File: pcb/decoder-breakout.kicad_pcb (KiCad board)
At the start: 2 copper layers, 1 part, among them U1 LS7866-S

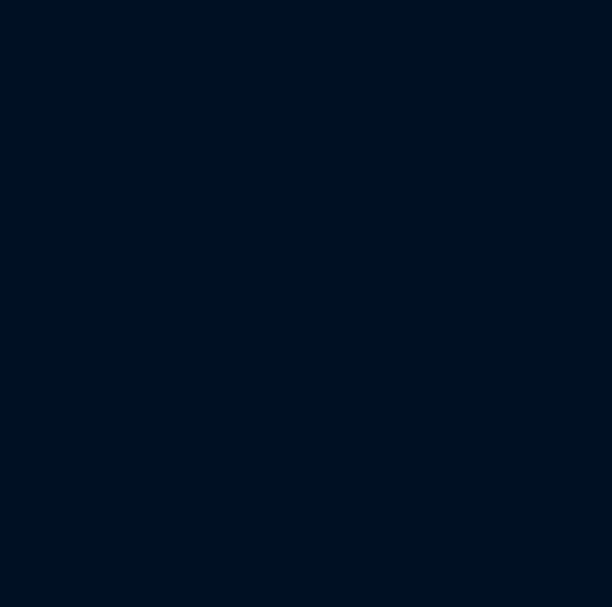
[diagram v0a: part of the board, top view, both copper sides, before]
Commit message: add resistors and jumpers
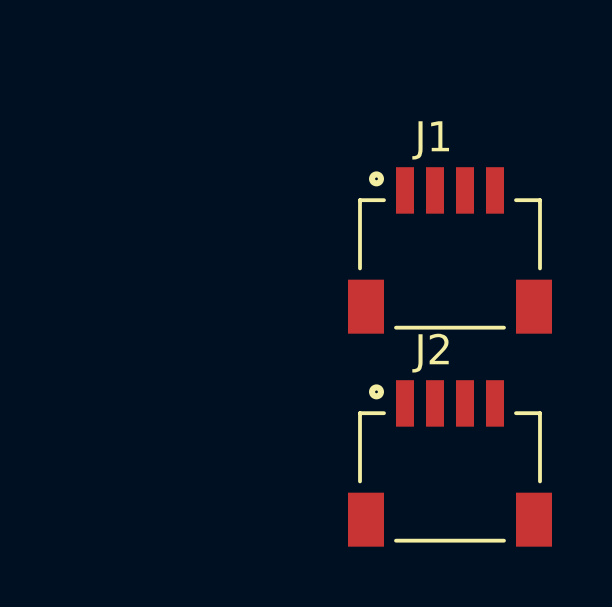
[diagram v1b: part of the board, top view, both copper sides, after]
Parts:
- added J1: SM04B-SRSS-TB_LF__SN_, SM04B-SRSS-TB(LF)(SN):JST_SM04B-SRSS-TB_LF__SN_, F.Cu at (169.9, 83.0)
- added J2: SM04B-SRSS-TB_LF__SN_, SM04B-SRSS-TB(LF)(SN):JST_SM04B-SRSS-TB_LF__SN_, F.Cu at (169.9, 90.1)
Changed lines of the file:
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@@
   (net 13 "unconnected-(U1-~{DFLAG}-Pad13)")
   (net 14 "unconnected-(U1-VDD-Pad14)")
+  (net 15 "unconnected-(J1-Pad1)")
+  (net 16 "unconnected-(J1-Pad2)")
+  (net 17 "unconnected-(J1-Pad3)")
+  (net 18 "unconnected-(J1-Pad4)")
+  (net 19 "Net-(J1-SHIELD-PadS1)")
+  (net 20 "unconnected-(J2-Pad1)")
+  (net 21 "unconnected-(J2-Pad2)")
+  (net 22 "unconnected-(J2-Pad3)")
+  (net 23 "unconnected-(J2-Pad4)")
+  (net 24 "Net-(J2-SHIELD-PadS1)")
   (footprint "LS7866-S:SOIC127P600X175-14N" (layer "F.Cu")
     (at 139.785 85.09)
@@
     (pad "14" smd roundrect (at 2.455 -3.81) (size 1.9 0.6) (layers "F.Cu" "F.Paste" "F.Mask") (roundrect_rratio 0.07)
       (net 14 "unconnected-(U1-VDD-Pad14)") (pinfunction "VDD") (pintype "power_in") (solder_mask_margin 0.102))
+    (model "${KIPRJMOD}/LS7866-S/LS7866-S--3DModel-STEP-56544.STEP"
+      (offset (xyz 0 0 0))
+      (scale (xyz 1 1 1))
+      (rotate (xyz -90 0 0))
+    )
+  )
+  (footprint "SM04B-SRSS-TB(LF)(SN):JST_SM04B-SRSS-TB_LF__SN_" (layer "F.Cu")
+    (at 169.92 90.105)
+    (property "Availability" "In Stock")
+    (property "Check_prices" "https://www.snapeda.com/parts/SM04B-SRSS-TB(LF)(SN)/JST+Sales+America+Inc./view-part/?ref=eda")
+    (property "Description" "\nConnector Header Surface Mount, Right Angle 4 position 0.039 (1.00mm)\n")
+    (property "MANUFACTURER" "JST")
+    (property "MF" "JST Sales")
+    (property "MP" "SM04B-SRSS-TB(LF)(SN)")
+    (property "Package" "None")
+    (property "Price" "None")
+    (property "STANDARD" "Manufacturer recommendations")
+    (property "Sheetfile" "decoder-breakout.kicad_sch")
+    (property "Sheetname" "")
+    (property "SnapEDA_Link" "https://www.snapeda.com/parts/SM04B-SRSS-TB(LF)(SN)/JST+Sales+America+Inc./view-part/?ref=snap")
+    (attr smd)
+    (fp_text reference "J2" (at -0.545095 -1.767685) (layer "F.SilkS")
+        (effects (font (size 1.001173 1.001173) (thickness 0.15)))
+    )
+    (fp_text value "SM04B-SRSS-TB_LF__SN_" (at 12.17039 5.74055) (layer "F.Fab")
+        (effects (font (size 1.000567 1.000567) (thickness 0.15)))
+    )
+    (fp_line (start -3 0.325) (end -3 2.6)
+      (stroke (width 0.127) (type solid)) (layer "F.SilkS"))
+    (fp_line (start -2.2 0.325) (end -3 0.325)
+      (stroke (width 0.127) (type solid)) (layer "F.SilkS"))
+    (fp_line (start -1.8 4.575) (end 1.8 4.575)
+      (stroke (width 0.127) (type solid)) (layer "F.SilkS"))
+    (fp_line (start 2.2 0.325) (end 3 0.325)
+      (stroke (width 0.127) (type solid)) (layer "F.SilkS"))
+    (fp_line (start 3 0.325) (end 3 2.6)
+      (stroke (width 0.127) (type solid)) (layer "F.SilkS"))
+    (fp_circle (center -2.45 -0.385) (end -2.35 -0.385)
+      (stroke (width 0.3) (type solid)) (fill none) (layer "F.SilkS"))
+    (fp_line (start -3.65 -1.025) (end 3.65 -1.025)
+      (stroke (width 0.05) (type solid)) (layer "F.CrtYd"))
+    (fp_line (start -3.65 5.025) (end -3.65 -1.025)
+      (stroke (width 0.05) (type solid)) (layer "F.CrtYd"))
+    (fp_line (start 3.65 -1.025) (end 3.65 5.025)
+      (stroke (width 0.05) (type solid)) (layer "F.CrtYd"))
+    (fp_line (start 3.65 5.025) (end -3.65 5.025)
+      (stroke (width 0.05) (type solid)) (layer "F.CrtYd"))
+    (fp_line (start -3 0.325) (end 3 0.325)
+      (stroke (width 0.127) (type solid)) (layer "F.Fab"))
+    (fp_line (start -3 4.575) (end -3 0.325)
+      (stroke (width 0.127) (type solid)) (layer "F.Fab"))
+    (fp_line (start 3 0.325) (end 3 4.575)
+      (stroke (width 0.127) (type solid)) (layer "F.Fab"))
+    (fp_line (start 3 4.575) (end -3 4.575)
+      (stroke (width 0.127) (type solid)) (layer "F.Fab"))
+    (fp_circle (center -2.45 -0.385) (end -2.35 -0.385)
+      (stroke (width 0.3) (type solid)) (fill none) (layer "F.Fab"))
+    (pad "1" smd rect (at -1.5 0) (size 0.6 1.55) (layers "F.Cu" "F.Paste" "F.Mask")
+      (net 20 "unconnected-(J2-Pad1)") (pinfunction "1") (pintype "passive") (solder_mask_margin 0.102))
+    (pad "2" smd rect (at -0.5 0) (size 0.6 1.55) (layers "F.Cu" "F.Paste" "F.Mask")
+      (net 21 "unconnected-(J2-Pad2)") (pinfunction "2") (pintype "passive") (solder_mask_margin 0.102))
+    (pad "3" smd rect (at 0.5 0) (size 0.6 1.55) (layers "F.Cu" "F.Paste" "F.Mask")
+      (net 22 "unconnected-(J2-Pad3)") (pinfunction "3") (pintype "passive") (solder_mask_margin 0.102))
+    (pad "4" smd rect (at 1.5 0) (size 0.6 1.55) (layers "F.Cu" "F.Paste" "F.Mask")
+      (net 23 "unconnected-(J2-Pad4)") (pinfunction "4") (pintype "passive") (solder_mask_margin 0.102))
+    (pad "S1" smd rect (at -2.8 3.875 180) (size 1.2 1.8) (layers "F.Cu" "F.Paste" "F.Mask")
+      (net 24 "Net-(J2-SHIELD-PadS1)") (pinfunction "SHIELD") (pintype "passive") (solder_mask_margin 0.102))
+    (pad "S2" smd rect (at 2.8 3.875 180) (size 1.2 1.8) (layers "F.Cu" "F.Paste" "F.Mask")
+      (net 24 "Net-(J2-SHIELD-PadS1)") (pinfunction "SHIELD") (pintype "passive") (solder_mask_margin 0.102))
+    (model "${KIPRJMOD}/SM04B-SRSS-TB(LF)(SN)/SM04B-SRSS-TB_LF__SN_.step"
+      (offset (xyz 0 0 -0.3))
+      (scale (xyz 1 1 1))
+      (rotate (xyz -90 0 0))
+    )
+  )
+  (footprint "SM04B-SRSS-TB(LF)(SN):JST_SM04B-SRSS-TB_LF__SN_" (layer "F.Cu")
+    (at 169.92 83.005)
+    (property "Availability" "In Stock")
+    (property "Check_prices" "https://www.snapeda.com/parts/SM04B-SRSS-TB(LF)(SN)/JST+Sales+America+Inc./view-part/?ref=eda")
+    (property "Description" "\nConnector Header Surface Mount, Right Angle 4 position 0.039 (1.00mm)\n")
+    (property "MANUFACTURER" "JST")
+    (property "MF" "JST Sales")
+    (property "MP" "SM04B-SRSS-TB(LF)(SN)")
+    (property "Package" "None")
+    (property "Price" "None")
+    (property "STANDARD" "Manufacturer recommendations")
+    (property "Sheetfile" "decoder-breakout.kicad_sch")
+    (property "Sheetname" "")
+    (property "SnapEDA_Link" "https://www.snapeda.com/parts/SM04B-SRSS-TB(LF)(SN)/JST+Sales+America+Inc./view-part/?ref=snap")
+    (attr smd)
+    (fp_text reference "J1" (at -0.545095 -1.767685) (layer "F.SilkS")
+        (effects (font (size 1.001173 1.001173) (thickness 0.15)))
+    )
+    (fp_text value "SM04B-SRSS-TB_LF__SN_" (at 12.17039 5.74055) (layer "F.Fab")
+        (effects (font (size 1.000567 1.000567) (thickness 0.15)))
+    )
+    (fp_line (start -3 0.325) (end -3 2.6)
+      (stroke (width 0.127) (type solid)) (layer "F.SilkS"))
+    (fp_line (start -2.2 0.325) (end -3 0.325)
+      (stroke (width 0.127) (type solid)) (layer "F.SilkS"))
+    (fp_line (start -1.8 4.575) (end 1.8 4.575)
+      (stroke (width 0.127) (type solid)) (layer "F.SilkS"))
+    (fp_line (start 2.2 0.325) (end 3 0.325)
+      (stroke (width 0.127) (type solid)) (layer "F.SilkS"))
+    (fp_line (start 3 0.325) (end 3 2.6)
+      (stroke (width 0.127) (type solid)) (layer "F.SilkS"))
+    (fp_circle (center -2.45 -0.385) (end -2.35 -0.385)
+      (stroke (width 0.3) (type solid)) (fill none) (layer "F.SilkS"))
+    (fp_line (start -3.65 -1.025) (end 3.65 -1.025)
+      (stroke (width 0.05) (type solid)) (layer "F.CrtYd"))
+    (fp_line (start -3.65 5.025) (end -3.65 -1.025)
+      (stroke (width 0.05) (type solid)) (layer "F.CrtYd"))
+    (fp_line (start 3.65 -1.025) (end 3.65 5.025)
+      (stroke (width 0.05) (type solid)) (layer "F.CrtYd"))
+    (fp_line (start 3.65 5.025) (end -3.65 5.025)
+      (stroke (width 0.05) (type solid)) (layer "F.CrtYd"))
+    (fp_line (start -3 0.325) (end 3 0.325)
+      (stroke (width 0.127) (type solid)) (layer "F.Fab"))
+    (fp_line (start -3 4.575) (end -3 0.325)
+      (stroke (width 0.127) (type solid)) (layer "F.Fab"))
+    (fp_line (start 3 0.325) (end 3 4.575)
+      (stroke (width 0.127) (type solid)) (layer "F.Fab"))
+    (fp_line (start 3 4.575) (end -3 4.575)
+      (stroke (width 0.127) (type solid)) (layer "F.Fab"))
+    (fp_circle (center -2.45 -0.385) (end -2.35 -0.385)
+      (stroke (width 0.3) (type solid)) (fill none) (layer "F.Fab"))
+    (pad "1" smd rect (at -1.5 0) (size 0.6 1.55) (layers "F.Cu" "F.Paste" "F.Mask")
+      (net 15 "unconnected-(J1-Pad1)") (pinfunction "1") (pintype "passive") (solder_mask_margin 0.102))
+    (pad "2" smd rect (at -0.5 0) (size 0.6 1.55) (layers "F.Cu" "F.Paste" "F.Mask")
+      (net 16 "unconnected-(J1-Pad2)") (pinfunction "2") (pintype "passive") (solder_mask_margin 0.102))
+    (pad "3" smd rect (at 0.5 0) (size 0.6 1.55) (layers "F.Cu" "F.Paste" "F.Mask")
+      (net 17 "unconnected-(J1-Pad3)") (pinfunction "3") (pintype "passive") (solder_mask_margin 0.102))
+    (pad "4" smd rect (at 1.5 0) (size 0.6 1.55) (layers "F.Cu" "F.Paste" "F.Mask")
+      (net 18 "unconnected-(J1-Pad4)") (pinfunction "4") (pintype "passive") (solder_mask_margin 0.102))
+    (pad "S1" smd rect (at -2.8 3.875 180) (size 1.2 1.8) (layers "F.Cu" "F.Paste" "F.Mask")
+      (net 19 "Net-(J1-SHIELD-PadS1)") (pinfunction "SHIELD") (pintype "passive") (solder_mask_margin 0.102))
+    (pad "S2" smd rect (at 2.8 3.875 180) (size 1.2 1.8) (layers "F.Cu" "F.Paste" "F.Mask")
+      (net 19 "Net-(J1-SHIELD-PadS1)") (pinfunction "SHIELD") (pintype "passive") (solder_mask_margin 0.102))
+    (model "${KIPRJMOD}/SM04B-SRSS-TB(LF)(SN)/SM04B-SRSS-TB_LF__SN_.step"
+      (offset (xyz 0 0 -0.3))
+      (scale (xyz 1 1 1))
+      (rotate (xyz -90 0 0))
+    )
   )
 )

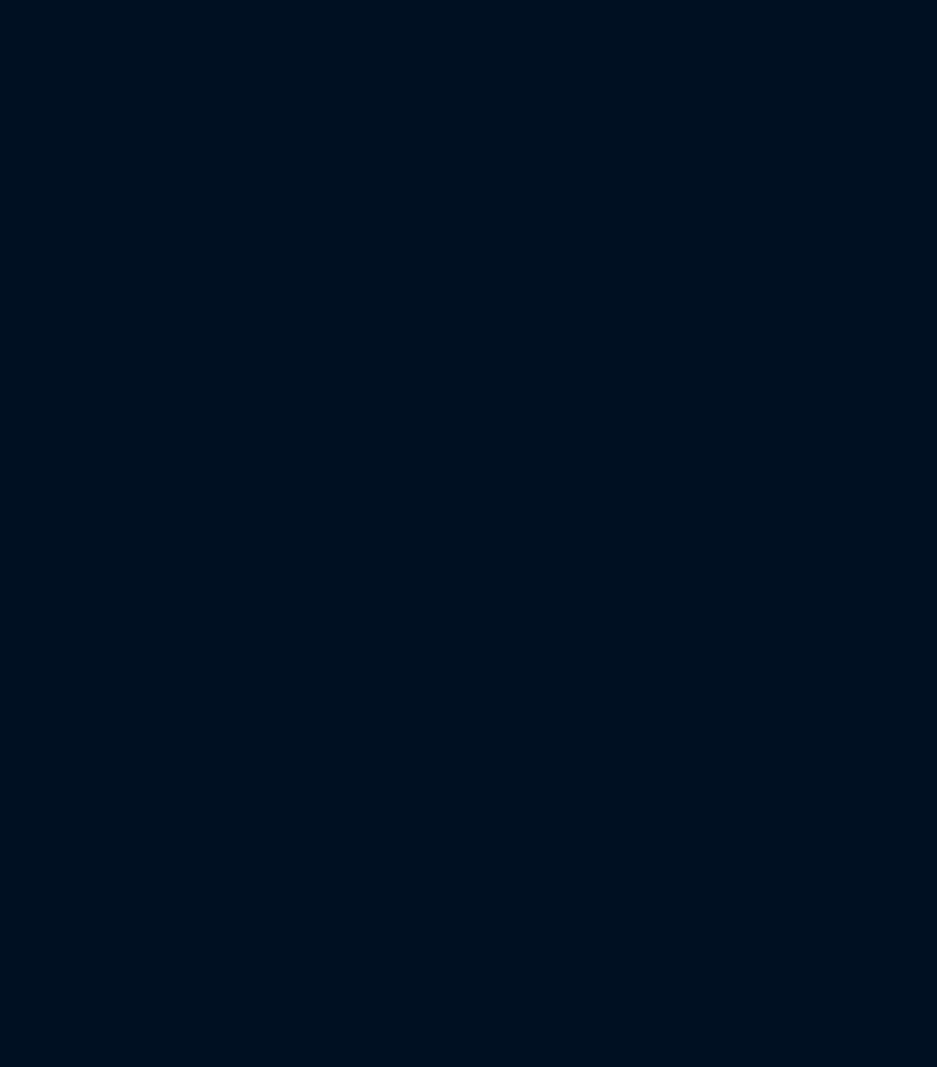
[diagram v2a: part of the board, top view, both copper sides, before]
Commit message: added terminal block, started on PCB
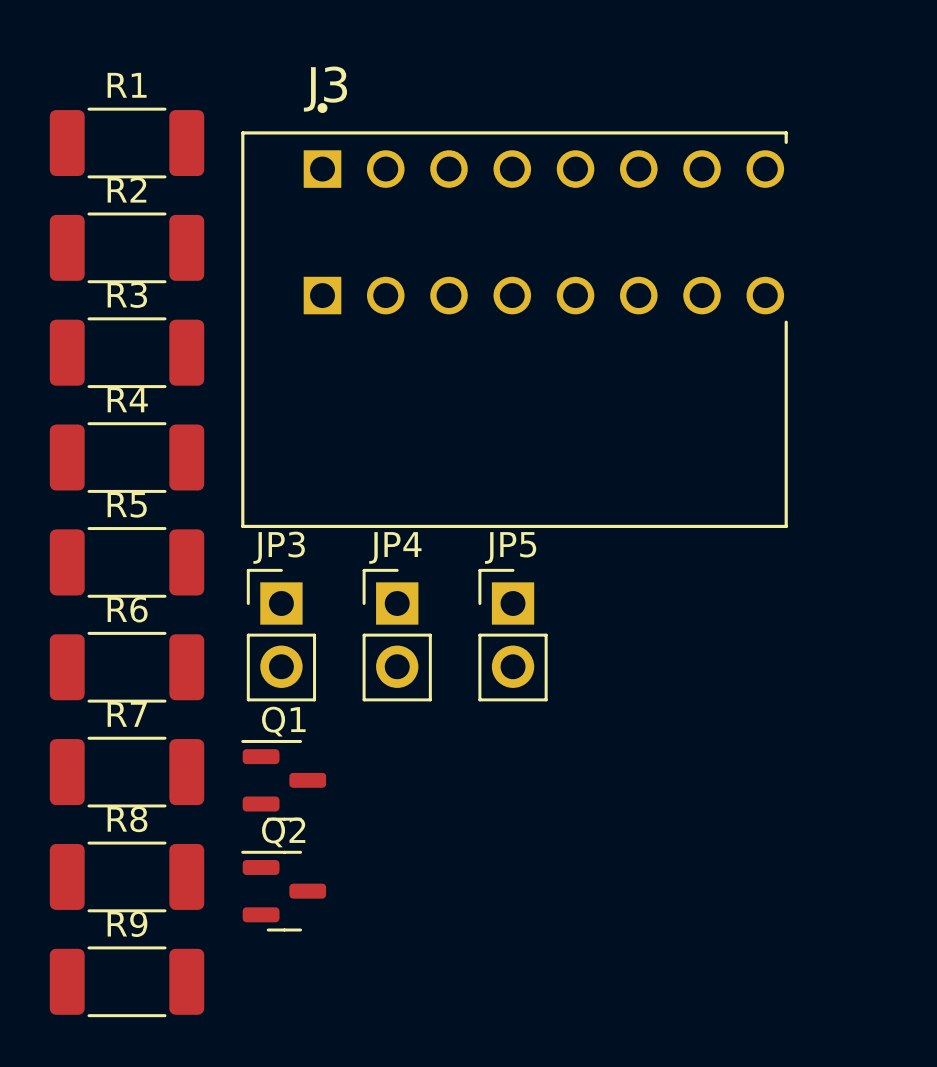
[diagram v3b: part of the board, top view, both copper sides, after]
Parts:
- added J3: TBL009-254-08GY-2GY, TBL009-254-08GY-2GY:CUI_TBL009-254-08GY-2GY, F.Cu at (106.7, 79.1)
- added JP3: Jumper_2_Bridged, Connector_PinHeader_2.54mm:PinHeader_1x02_P2.54mm_Vertical, F.Cu at (105.0, 96.5)
- added JP4: Jumper_2_Bridged, Connector_PinHeader_2.54mm:PinHeader_1x02_P2.54mm_Vertical, F.Cu at (109.7, 96.5)
- added JP5: Jumper_2_Bridged, Connector_PinHeader_2.54mm:PinHeader_1x02_P2.54mm_Vertical, F.Cu at (114.3, 96.5)
- added Q1: BSS138, Package_TO_SOT_SMD:SOT-23, F.Cu at (105.1, 103.6)
- added Q2: BSS138, Package_TO_SOT_SMD:SOT-23, F.Cu at (105.1, 108.1)
- added R1: 300, Resistor_SMD:R_2010_5025Metric_Pad1.40x2.65mm_HandSolder, F.Cu at (98.8, 78.0)
- added R2: 300, Resistor_SMD:R_2010_5025Metric_Pad1.40x2.65mm_HandSolder, F.Cu at (98.8, 82.2)
- added R3: 300, Resistor_SMD:R_2010_5025Metric_Pad1.40x2.65mm_HandSolder, F.Cu at (98.8, 86.5)
- added R4: 300, Resistor_SMD:R_2010_5025Metric_Pad1.40x2.65mm_HandSolder, F.Cu at (98.8, 90.7)
- added R5: 300, Resistor_SMD:R_2010_5025Metric_Pad1.40x2.65mm_HandSolder, F.Cu at (98.8, 94.9)
- added R6: 10k, Resistor_SMD:R_2010_5025Metric_Pad1.40x2.65mm_HandSolder, F.Cu at (98.8, 99.1)
- added R7: 10k, Resistor_SMD:R_2010_5025Metric_Pad1.40x2.65mm_HandSolder, F.Cu at (98.8, 103.3)
- added R8: 10k, Resistor_SMD:R_2010_5025Metric_Pad1.40x2.65mm_HandSolder, F.Cu at (98.8, 107.5)
- added R9: 10k, Resistor_SMD:R_2010_5025Metric_Pad1.40x2.65mm_HandSolder, F.Cu at (98.8, 111.7)
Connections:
- J1 pad 1: unconnected-(J1-Pad1) -> GND
- J1 pad 2: unconnected-(J1-Pad2) -> VDD
- J1 pad 3: unconnected-(J1-Pad3) -> Net-(U1-SDA)
- J1 pad 4: unconnected-(J1-Pad4) -> Net-(U1-SCL)
- J1 pad S1: Net-(J1-SHIELD-PadS1) -> GND
- J1 pad S2: Net-(J1-SHIELD-PadS1) -> GND
- J2 pad 1: unconnected-(J2-Pad1) -> GND
- J2 pad 2: unconnected-(J2-Pad2) -> VDD
- J2 pad 3: unconnected-(J2-Pad3) -> Net-(U1-SDA)
- J2 pad 4: unconnected-(J2-Pad4) -> Net-(U1-SCL)
- J2 pad S1: Net-(J2-SHIELD-PadS1) -> GND
- J2 pad S2: Net-(J2-SHIELD-PadS1) -> GND
- U1 pad 1: unconnected-(U1-A-Pad1) -> A
- U1 pad 10: unconnected-(U1-A2-Pad10) -> Net-(U1-A2)
- U1 pad 14: unconnected-(U1-VDD-Pad14) -> VDD
- U1 pad 2: unconnected-(U1-B-Pad2) -> B
- U1 pad 3: unconnected-(U1-Z-Pad3) -> Net-(U1-Z)
- U1 pad 4: unconnected-(U1-CE-Pad4) -> Net-(U1-CE)
- U1 pad 5: unconnected-(U1-SCL-Pad5) -> Net-(U1-SCL)
- U1 pad 6: unconnected-(U1-SDA-Pad6) -> Net-(U1-SDA)
- U1 pad 7: unconnected-(U1-VSS-Pad7) -> GND
- U1 pad 8: unconnected-(U1-A0-Pad8) -> Net-(U1-A0)
- U1 pad 9: unconnected-(U1-A1-Pad9) -> Net-(U1-A1)

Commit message: pcb rough layout
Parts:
- moved J1 75.7 mm to (94.7, 91.4), turned to -90 degrees
- moved R1 52.8 mm to (146.2, 101.2)
- moved R2 52.8 mm to (146.2, 105.4)
- moved R5 46.1 mm to (144.8, 91.4), turned to 90 degrees
- moved R4 40.9 mm to (139.7, 91.4), turned to 90 degrees
- moved R3 36.2 mm to (134.6, 91.4), turned to 90 degrees
- moved JP5 34.1 mm to (144.8, 81.3)
- moved JP4 33.7 mm to (139.7, 81.3)
- moved JP3 33.3 mm to (134.6, 81.3)
- moved R6 20.6 mm to (119.4, 100.3)
- moved R8 20.6 mm to (119.4, 106.7)
- moved U1 20.6 mm to (132.0, 104.1)
- moved J3 20.3 mm to (122.0, 92.3), turned to 180 degrees
- moved J2 18.1 mm to (151.9, 91.4), turned to 90 degrees
- moved R9 9.35 mm to (106.7, 106.7)
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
